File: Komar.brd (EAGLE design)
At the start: 58 x 58 mm, 109 parts, among them CON1 USB-VERTICAL, CON2 PINHEAD_1X01-2, CON3 CON-4P-TABS-STRAIGHT, CON4 CON-4P-TABS-STRAIGHT, CON5 CON-4P-TABS-STRAIGHT, CON6 CON-4P-TABS-STRAIGHT, CON7 CON-4P-TABS-STRAIGHT, CON8 CON-6P-SM06B, CON9 PINHEAD_1X01-2, IC1 TPD3S014DBVR-SOT23-6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

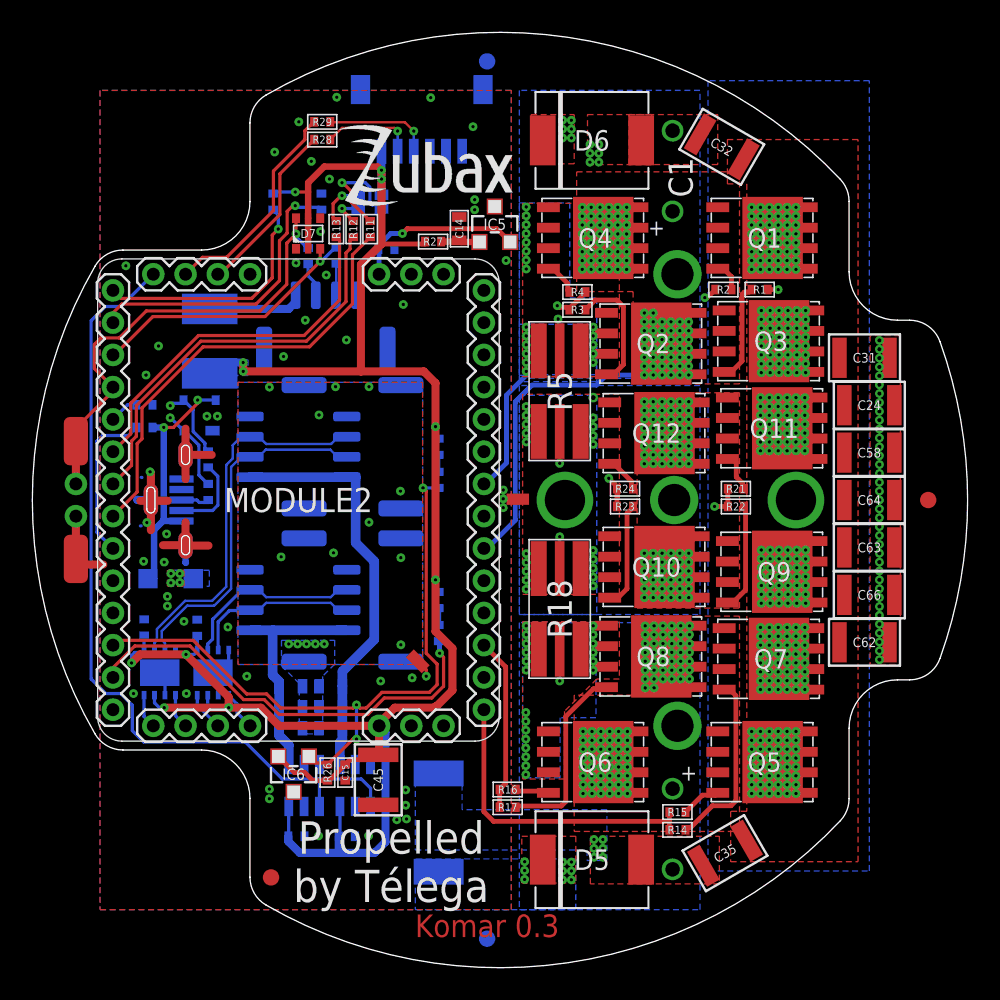
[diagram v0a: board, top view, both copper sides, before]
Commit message: CAN transcievers rerouting
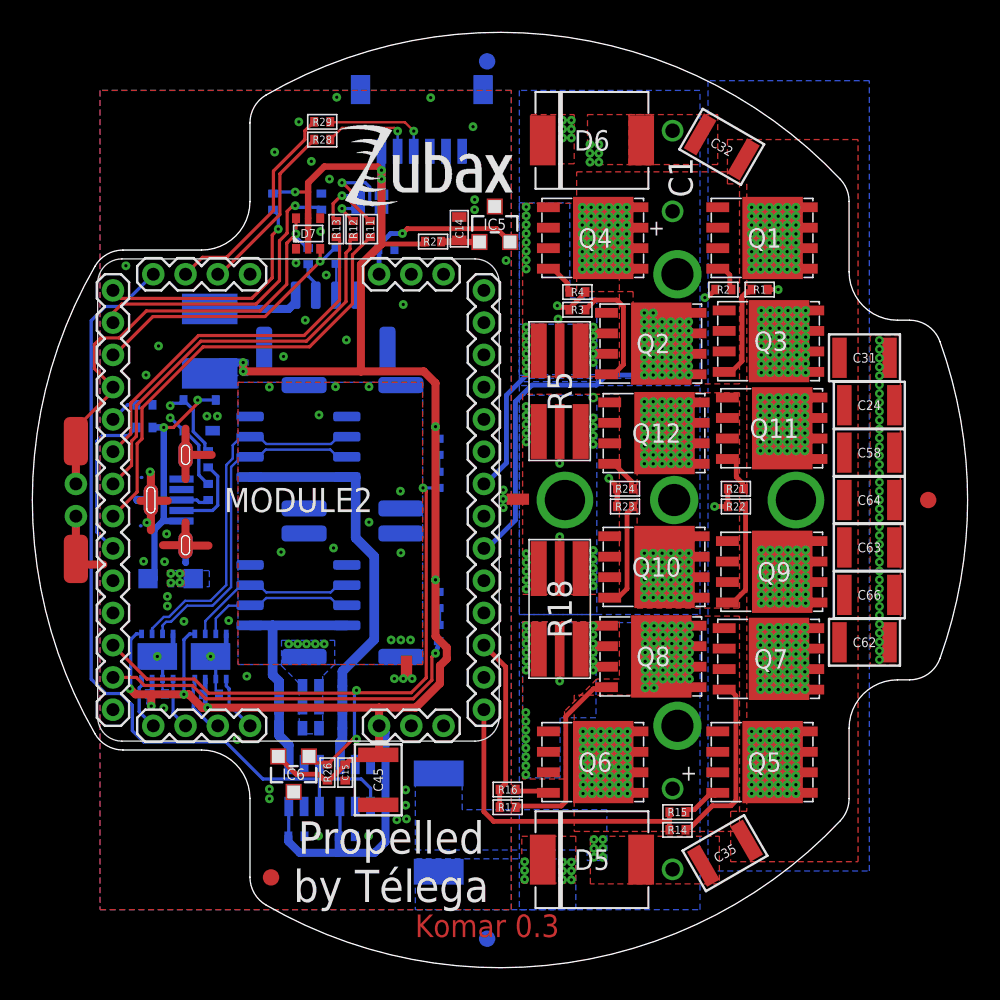
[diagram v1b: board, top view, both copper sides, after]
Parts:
- MODULE2: value MITOHONDRIQUE_V0.2-TH -> MITOCHONDRIK_LV-TH; device zubax_modules:MITOHONDRIQUE-TH -> zubax_modules:MITOHONDRIK-TH
- moved C11 5.87 mm to (11.1, 16.9), turned to 180 degrees
- moved C12 4.80 mm to (7.72, 17.0), turned to 180 degrees
- moved IC4 1.01 mm to (7.75, 19.3)
- moved IC3 1.01 mm to (11.1, 19.3)
- moved U$1 0.78 mm to (23.2, 18.6), turned to 90 degrees
- moved CON3 0.30 mm to (22.4, 23.1)
- moved CON4 0.30 mm to (16.4, 23.1)
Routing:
- net CAN2_LED: track 27.1 -> 23.4 mm
- net GND: track 34.7 -> 38.3 mm, vias 48 -> 50
- net VDD_5V: track 147.7 -> 146.1 mm
- net CAN1_RX: track 2.43 -> 3.81 mm
- net CAN1_LED: track 42.2 -> 41.0 mm
- net CAN2_RX: track 2.14 -> 3.32 mm
- net CAN2_TX: track 2.16 -> 3.22 mm
- net CAN1_TX: track 2.45 -> 3.51 mm
- net N$46: track 22.0 -> 21.0 mm
- net N$44: track 23.4 -> 22.5 mm
- net N$21: track 10.4 -> 9.79 mm
- net N$22: track 11.5 -> 10.9 mm

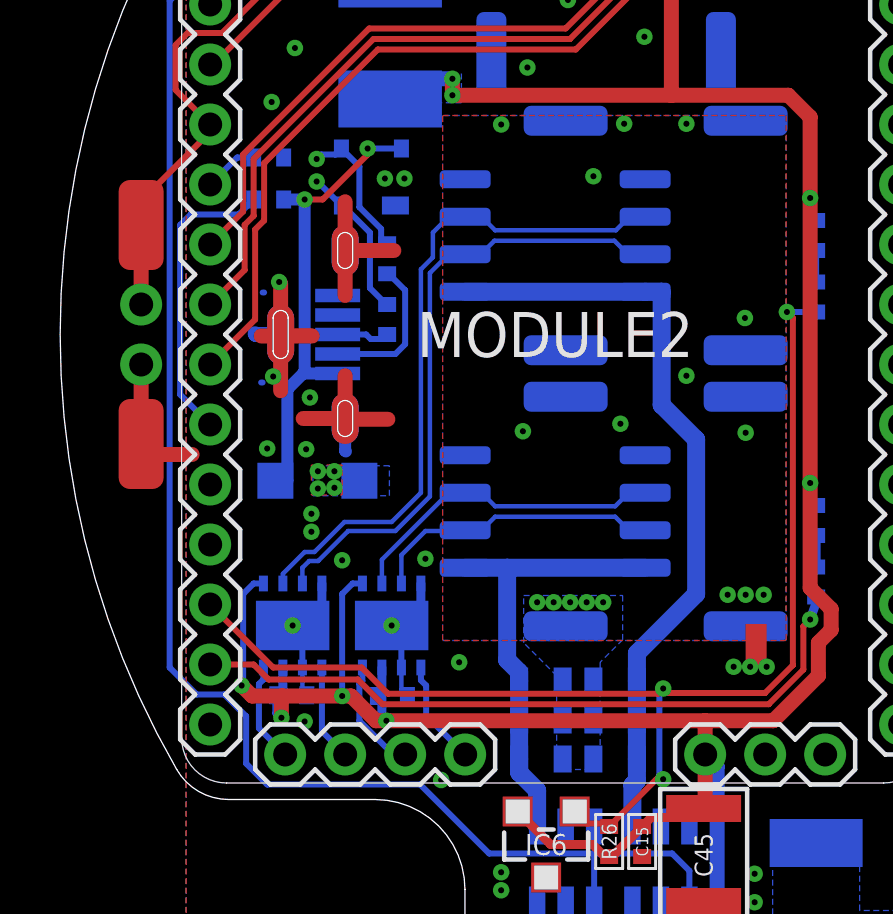
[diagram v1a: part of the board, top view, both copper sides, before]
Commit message: Redundant thermistor pads removed
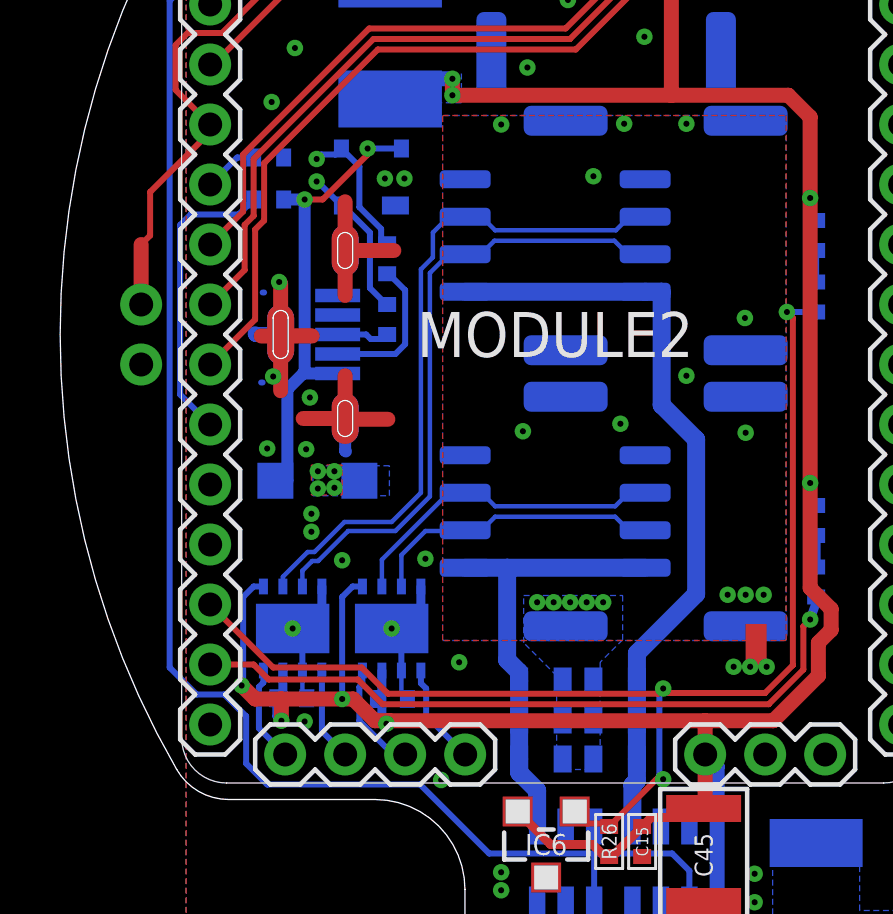
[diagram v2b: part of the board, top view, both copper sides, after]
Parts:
- removed PAD6, PAD7: PAD-3X1.5, PADS:3X1.5
- moved C12 0.10 mm to (7.72, 16.9)
- moved IC3 0.10 mm to (11.1, 19.2)
- moved IC4 0.10 mm to (7.75, 19.2)
- moved C11 0.10 mm to (11.1, 16.9)
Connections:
- net GND: no longer PAD6.P$1
- net GPIO1: no longer PAD7.P$1
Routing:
- net GND: track 38.3 -> 33.8 mm
- net GPIO1: track 29.8 -> 29.1 mm

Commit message: width updates
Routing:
- net GND: track 33.8 -> 36.9 mm
- net PHASE_C: track 15.7 -> 15.1 mm
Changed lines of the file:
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@@
 <setting verticaltext="up"/>
 </settings>
-<grid distance="0.1" unitdist="mm" unit="mm" style="lines" multiple="1" display="yes" altdistance="0.1" altunitdist="mm" altunit="mm"/>
+<grid distance="1" unitdist="mm" unit="mm" style="lines" multiple="1" display="yes" altdistance="0.1" altunitdist="mm" altunit="mm"/>
 <layers>
-<layer number="1" name="Top" color="4" fill="1" visible="no" active="yes"/>
+<layer number="1" name="Top" color="4" fill="1" visible="yes" active="yes"/>
 <layer number="2" name="Route2" color="1" fill="3" visible="no" active="yes"/>
 <layer number="3" name="Route3" color="4" fill="3" visible="no" active="yes"/>
@@
 <layer number="19" name="Unrouted" color="6" fill="1" visible="yes" active="yes"/>
 <layer number="20" name="Dimension" color="24" fill="1" visible="yes" active="yes"/>
-<layer number="21" name="tPlace" color="7" fill="1" visible="no" active="yes"/>
+<layer number="21" name="tPlace" color="7" fill="1" visible="yes" active="yes"/>
 <layer number="22" name="bPlace" color="7" fill="1" visible="yes" active="yes"/>
-<layer number="23" name="tOrigins" color="15" fill="1" visible="no" active="yes"/>
+<layer number="23" name="tOrigins" color="15" fill="1" visible="yes" active="yes"/>
 <layer number="24" name="bOrigins" color="15" fill="1" visible="yes" active="yes"/>
-<layer number="25" name="tNames" color="7" fill="1" visible="no" active="yes"/>
+<layer number="25" name="tNames" color="7" fill="1" visible="yes" active="yes"/>
 <layer number="26" name="bNames" color="7" fill="1" visible="yes" active="yes"/>
 <layer number="27" name="tValues" color="7" fill="1" visible="no" active="yes"/>
@@
 <layer number="49" name="Reference" color="7" fill="1" visible="no" active="yes"/>
 <layer number="50" name="dxf" color="7" fill="1" visible="no" active="no"/>
-<layer number="51" name="tDocu" color="7" fill="1" visible="no" active="yes"/>
+<layer number="51" name="tDocu" color="7" fill="1" visible="yes" active="yes"/>
 <layer number="52" name="bDocu" color="7" fill="1" visible="yes" active="yes"/>
 <layer number="53" name="tGND_GNDA" color="7" fill="9" visible="no" active="no"/>
@@
 <via x="12.7" y="14.15" extent="1-16" drill="0.2" diameter="0.55"/>
 <via x="8.15" y="16.1" extent="1-16" drill="0.2" diameter="0.55"/>
+<wire x1="2.7" y1="28" x2="3.7" y2="27" width="0.3" layer="1"/>
+<wire x1="3.7" y1="27" x2="5.4" y2="27" width="0.3" layer="1"/>
 <wire x1="9.5" y1="31.8" x2="9.5" y2="31.8" width="0" layer="19" extent="1-16"/>
 <wire x1="9.35" y1="31.8" x2="9.5" y2="31.8" width="0" layer="19" extent="1-1"/>
-<wire x1="2.7" y1="28" x2="6.5" y2="29.025" width="0" layer="19" extent="16-16"/>
 </signal>
 <signal name="PHASE_A_GND">
@@
 <contactref element="MODULE2" pad="8"/>
 <via x="30.625" y="39.175" extent="1-16" drill="0.2" diameter="0.55"/>
-<wire x1="30.45" y1="39" x2="30.625" y2="39.175" width="0.2" layer="1"/>
 <wire x1="28" y1="30" x2="28.1" y2="30" width="0.3" layer="16"/>
 <wire x1="28.1" y1="30" x2="29.4" y2="31.3" width="0.3" layer="16"/>
-<wire x1="29.4" y1="31.3" x2="29.4" y2="35.50281875" width="0.3" layer="16"/>
-<wire x1="29.4" y1="35.50281875" x2="30.625" y2="36.72781875" width="0.3" layer="16"/>
+<wire x1="29.4" y1="35.75" x2="30.625" y2="36.975" width="0.3" layer="16"/>
+<wire x1="29.4" y1="31.3" x2="29.4" y2="35.75" width="0.3" layer="16"/>
 </signal>
 <signal name="PHASE_B_CURRENT_SHUNT_N">
@@
 <contactref element="Q10" pad="8"/>
 <contactref element="Q10" pad="P$1"/>
-<wire x1="37.5" y1="35.55" x2="37.95" y2="35.1" width="0.3" layer="1"/>
 <wire x1="28" y1="34" x2="26.95" y2="35.05" width="0.2" layer="15"/>
 <wire x1="26.95" y1="35.05" x2="26.95" y2="36.29350625" width="0.2" layer="15"/>
@@
 <contactref element="D7" pad="6"/>
 <contactref element="CON2" pad="1"/>
-<wire x1="2.7" y1="30" x2="2.7" y2="32" width="0.5" layer="1"/>
 <via x="16.35" y="45.5" extent="1-16" drill="0.2" diameter="0.55"/>
 <wire x1="16.35" y1="45.5" x2="16.35" y2="46.475" width="0.2" layer="1"/>
@@
 <wire x1="15.775" y1="44.925" x2="15.775" y2="42.375" width="0.2" layer="1"/>
 <contactref element="MODULE2" pad="25"/>
-<wire x1="5" y1="36" x2="5" y2="35.75" width="0.2" layer="1"/>
-<wire x1="5" y1="35.75" x2="3" y2="33.75" width="0.2" layer="1"/>
-<wire x1="3" y1="33.75" x2="3" y2="32.3" width="0.2" layer="1"/>
-<wire x1="3" y1="32.3" x2="2.7" y2="32" width="0.2" layer="1"/>
-<wire x1="5.39350625" y1="39.05" x2="4.25" y2="39.05" width="0.2" layer="1"/>
-<wire x1="7.06850625" y1="40.725" x2="5.39350625" y2="39.05" width="0.2" layer="1"/>
-<wire x1="4.25" y1="39.05" x2="3.85" y2="38.65" width="0.2" layer="1"/>
-<wire x1="3.85" y1="37.15" x2="5" y2="36" width="0.2" layer="1"/>
-<wire x1="14.125" y1="40.725" x2="7.06850625" y2="40.725" width="0.2" layer="1"/>
-<wire x1="3.85" y1="38.65" x2="3.85" y2="37.15" width="0.2" layer="1"/>
+<wire x1="5" y1="36" x2="5" y2="35.55" width="0.2" layer="1"/>
+<wire x1="5" y1="35.55" x2="3.8" y2="34.35" width="0.2" layer="1"/>
+<wire x1="5.49350625" y1="39.05" x2="4.55" y2="39.05" width="0.2" layer="1"/>
+<wire x1="7.16850625" y1="40.725" x2="5.49350625" y2="39.05" width="0.2" layer="1"/>
+<wire x1="4.55" y1="39.05" x2="3.95" y2="38.45" width="0.2" layer="1"/>
+<wire x1="5" y1="36.4" x2="5" y2="36" width="0.2" layer="1"/>
+<wire x1="5" y1="36.4" x2="3.95" y2="37.45" width="0.2" layer="1"/>
+<wire x1="14.125" y1="40.725" x2="7.16850625" y2="40.725" width="0.2" layer="1"/>
+<wire x1="3.95" y1="38.45" x2="3.95" y2="37.45" width="0.2" layer="1"/>
+<wire x1="3.8" y1="31.1" x2="2.7" y2="30" width="0.2" layer="1"/>
+<wire x1="3.8" y1="34.35" x2="3.8" y2="31.1" width="0.2" layer="1"/>
 </signal>
 <signal name="GAIN_OUT">
@@
 <signal name="GATE_ENABLE_OUT">
 <contactref element="LED4" pad="A"/>
-<wire x1="5.544975" y1="41.15" x2="13.869975" y2="41.15" width="0.2" layer="1"/>
-<wire x1="5" y1="40.605025" x2="5.544975" y2="41.15" width="0.2" layer="1"/>
+<wire x1="6.944975" y1="41.15" x2="13.869975" y2="41.15" width="0.2" layer="1"/>
+<wire x1="5" y1="40" x2="5.794975" y2="40" width="0.2" layer="1"/>
+<wire x1="6.944975" y1="41.15" x2="5.794975" y2="40" width="0.2" layer="1"/>
 <via x="16.3" y="47.25" extent="1-16" drill="0.2" diameter="0.55"/>
 <wire x1="13.869975" y1="41.15" x2="15.325" y2="42.605025" width="0.2" layer="1"/>
@@
 <wire x1="16.4" y1="47.15" x2="17.775" y2="47.15" width="0.2" layer="16"/>
 <contactref element="MODULE2" pad="23"/>
-<wire x1="5" y1="40" x2="5" y2="40.605025" width="0.2" layer="1"/>
 </signal>
 <signal name="UART_RX">

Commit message: minor attribute extension
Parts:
- added U$2: (no value), logo:YOBA_17X17
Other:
- board text added: "CON100"
- board text added: "CON101"
- board text added: "CON102"
- board text added: "CON103"
- board text added: "CON104"
- board text added: "CON105"
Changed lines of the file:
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@@
 <setting verticaltext="up"/>
 </settings>
-<grid distance="1" unitdist="mm" unit="mm" style="lines" multiple="1" display="yes" altdistance="0.1" altunitdist="mm" altunit="mm"/>
+<grid distance="0.5" unitdist="mm" unit="mm" style="lines" multiple="1" display="yes" altdistance="0.1" altunitdist="mm" altunit="mm"/>
 <layers>
 <layer number="1" name="Top" color="4" fill="1" visible="yes" active="yes"/>
@@
 <layer number="14" name="Route14" color="1" fill="6" visible="no" active="no"/>
 <layer number="15" name="Route15" color="4" fill="6" visible="no" active="yes"/>
-<layer number="16" name="Bottom" color="9" fill="1" visible="yes" active="yes"/>
+<layer number="16" name="Bottom" color="9" fill="1" visible="no" active="yes"/>
 <layer number="17" name="Pads" color="2" fill="1" visible="yes" active="yes"/>
 <layer number="18" name="Vias" color="2" fill="1" visible="yes" active="yes"/>
@@
 <layer number="20" name="Dimension" color="24" fill="1" visible="yes" active="yes"/>
 <layer number="21" name="tPlace" color="7" fill="1" visible="yes" active="yes"/>
-<layer number="22" name="bPlace" color="7" fill="1" visible="yes" active="yes"/>
+<layer number="22" name="bPlace" color="7" fill="1" visible="no" active="yes"/>
 <layer number="23" name="tOrigins" color="15" fill="1" visible="yes" active="yes"/>
-<layer number="24" name="bOrigins" color="15" fill="1" visible="yes" active="yes"/>
+<layer number="24" name="bOrigins" color="15" fill="1" visible="no" active="yes"/>
 <layer number="25" name="tNames" color="7" fill="1" visible="yes" active="yes"/>
-<layer number="26" name="bNames" color="7" fill="1" visible="yes" active="yes"/>
+<layer number="26" name="bNames" color="7" fill="1" visible="no" active="yes"/>
 <layer number="27" name="tValues" color="7" fill="1" visible="no" active="yes"/>
 <layer number="28" name="bValues" color="7" fill="1" visible="no" active="yes"/>
@@
 <layer number="50" name="dxf" color="7" fill="1" visible="no" active="no"/>
 <layer number="51" name="tDocu" color="7" fill="1" visible="yes" active="yes"/>
-<layer number="52" name="bDocu" color="7" fill="1" visible="yes" active="yes"/>
+<layer number="52" name="bDocu" color="7" fill="1" visible="no" active="yes"/>
 <layer number="53" name="tGND_GNDA" color="7" fill="9" visible="no" active="no"/>
 <layer number="54" name="bGND_GNDA" color="1" fill="9" visible="no" active="no"/>
@@
 </layers>
 <board>
+<fusionsync huburn="a.cGVyc29uYWw6dWUyYWE4ZDY4" projecturn="a.cGVyc29uYWw6dWUyYWE4ZDY4IzIwMTgxMDI3MTU2OTA4Mjgx" f3durn="urn:adsk.wipprod:dm.lineage:yua-ROE5Tb29pIDQe9ePEg" pcbguid="" lastpulledtime="" lastsyncedchangeguid="" latestrevisionid="99d9bd0f-ab10-4f4c-9d53-7a49861b2582" lastsyncedrevisionid="99d9bd0f-ab10-4f4c-9d53-7a49861b2582" lastboardhashguid="794f6e2b-7879-ceef-8c4b-03a35c66539a" lastpushedtime="2020-05-13T06:42:24Z" linktopcb3d="%12"/>
 <plain>
 <wire x1="29.2" y1="56.85" x2="29.2" y2="1.15" width="0.2" layer="22" style="shortdash"/>
@@
 <wire x1="50.0995" y1="9.1114" x2="50.6439" y2="10.483" width="0.01" layer="20" curve="43.299581"/>
 <wire x1="50.6439" y1="10.483" x2="50.6439" y2="14.85" width="0.01" layer="20"/>
+<text x="10.5" y="43" size="1" layer="25" font="vector" ratio="15" align="center">CON100</text>
+<text x="10.5" y="15" size="1" layer="25" font="vector" ratio="15" align="center">CON101</text>
+<text x="23.5" y="15" size="1" layer="25" font="vector" ratio="15" align="center">CON102</text>
+<text x="23.5" y="43" size="1" layer="25" font="vector" ratio="15" align="center">CON103</text>
+<text x="5" y="29" size="1" layer="25" font="vector" ratio="15" rot="R90" align="center">CON104</text>
+<text x="28" y="29" size="1" layer="25" font="vector" ratio="15" rot="R90" align="center">CON105</text>
 </plain>
 <attributes>
@@
 <attribute name="AEC-Q" value="AEC-Q200" x="11" y="38.85" size="1.778" layer="28" rot="MR270" display="off"/>
 <attribute name="DIGIKEY#" value="MF-MSMF010-2CT-ND" x="11" y="38.85" size="1.778" layer="28" rot="MR270" display="off"/>
+<attribute name="HOLD_CURRENT" value="100 mA" x="11" y="38.85" size="1.778" layer="28" rot="MR270" display="off"/>
 <attribute name="MANF" value="Bourns Inc." x="11" y="38.85" size="1.778" layer="28" rot="MR270" display="off"/>
 <attribute name="MANF#" value="MF-MSMF010-2" x="11" y="38.85" size="1.778" layer="28" rot="MR270" display="off"/>
 <attribute name="NAME" x="11" y="38.85" size="0.8" layer="26" font="vector" ratio="15" rot="MR270" align="center"/>
 <attribute name="PACKAGE" value="1812" x="4.525" y="38.525" size="1.778" layer="28" rot="MR270" display="off"/>
+<attribute name="TIME_TO_TRIP" value="1.5 S" x="11" y="38.85" size="1.778" layer="28" rot="MR270" display="off"/>
+<attribute name="TRIP_CURRENT" value="300 mA" x="11" y="38.85" size="1.778" layer="28" rot="MR270" display="off"/>
 </element>
 <element name="R8" library="rc" library_urn="urn:adsk.eagle:library:2539423" package="R0402" package3d_urn="urn:adsk.eagle:package:2539456/2" value="200R" x="17.1" y="44.125" smashed="yes" rot="MR270">
@@
 <attribute name="OPERATING_TEMP" value="-25°C ~ 85°C" x="18.2" y="38.8" size="1.778" layer="28" rot="MR180" display="off"/>
 </element>
-<element name="MODULE2" library="zubax_modules" library_urn="urn:adsk.eagle:library:5014895" package="MITOHONDRIK-TH" package3d_urn="urn:adsk.eagle:package:4410646/15" value="MITOCHONDRIK_LV-TH" x="16.5" y="29" smashed="yes" rot="R180">
+<element name="MODULE2" library="zubax_modules" library_urn="urn:adsk.eagle:library:5014895" package="MITOHONDRIK-TH" package3d_urn="urn:adsk.eagle:package:4410646/16" value="MITOCHONDRIK_LV-TH" x="16.5" y="29" smashed="yes" rot="R180">
 <attribute name="MANF" value="Zubax Robotics" x="16.5" y="29" size="1.778" layer="27" rot="R180" display="off"/>
 <attribute name="MANF#" value="Mitochondrik" x="16.5" y="29" size="1.778" layer="27" rot="R180" display="off"/>
-<attribute name="NAME" x="16.5" y="29" size="1.5" layer="21" font="vector" ratio="15" rot="R180" align="center"/>
 </element>
 <element name="IC6" library="misc" library_urn="urn:adsk.eagle:library:5347860" package="SOT23B-3" package3d_urn="urn:adsk.eagle:package:1040193/4" value="11LC040T-E/TT" x="16.2" y="12" smashed="yes" rot="R180">
@@
 <attribute name="TOLERANCE" value="5%" x="18.3" y="12.1" size="1.778" layer="27" rot="R270" display="off"/>
 </element>
+<element name="U$2" library="logo" library_urn="urn:adsk.eagle:library:20108282" package="YOBA_17X17" value="" x="10" y="21" smashed="yes"/>
 </elements>
 <signals>
@@
 </note>
 <note version="8.3" severity="warning">
+Since Version 8.3, EAGLE supports Fusion synchronisation.
+This feature will not be available in this version and saving
+the document will break the link to the Fusion PCB feature.
+</note>
+<note version="8.3" severity="warning">
